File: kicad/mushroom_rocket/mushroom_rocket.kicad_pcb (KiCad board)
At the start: 2 copper layers, 69.7 x 94.5 mm, 8 parts, among them SW1 SW_DIP_x01

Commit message: 2 fixes
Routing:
- added copper zone on F.Cu, net VCC
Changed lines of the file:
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@@
 		)
 		(fp_text user "+"
-			(at 3 -4.249999 10)
+			(at 3 -4.249998 10)
 			(layer "B.SilkS")
 			(effects
@@
 	)
 	(zone
+		(net 3)
+		(net_name "VCC")
+		(layer "F.Cu")
+		(hatch edge 0.5)
+		(priority 8)
+		(connect_pads
+			(clearance 0.5)
+		)
+		(min_thickness 0.25)
+		(filled_areas_thickness no)
+		(fill yes
+			(thermal_gap 0.5)
+			(thermal_bridge_width 0.5)
+		)
+		(polygon
+			(pts
+				(xy 154 73.374) (xy 157.75 73.374) (xy 157.75 74.25) (xy 153.995 74.308)
+			)
+		)
+	)
+	(zone
+		(net 2)
+		(net_name "GND")
+		(layer "F.Cu")
+		(hatch edge 0.5)
+		(priority 7)
+		(connect_pads
+			(clearance 0.5)
+		)
+		(min_thickness 0.25)
+		(filled_areas_thickness no)
+		(fill yes
+			(thermal_gap 0.5)
+			(thermal_bridge_width 0.5)
+		)
+		(polygon
+			(pts
+				(xy 156.5 126) (xy 157 129.5) (xy 158 130.5) (xy 158.5 130.5) (xy 160 129) (xy 160.25 126) (xy 158.5 125.5)
+			)
+		)
+	)
+	(zone

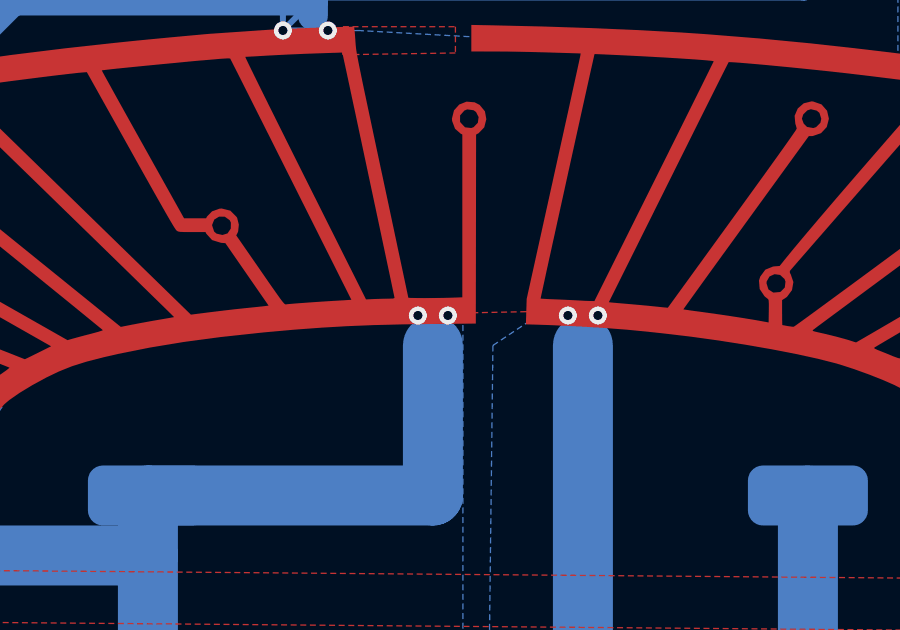
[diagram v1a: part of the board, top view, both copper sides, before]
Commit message: added a random pad into the footprint
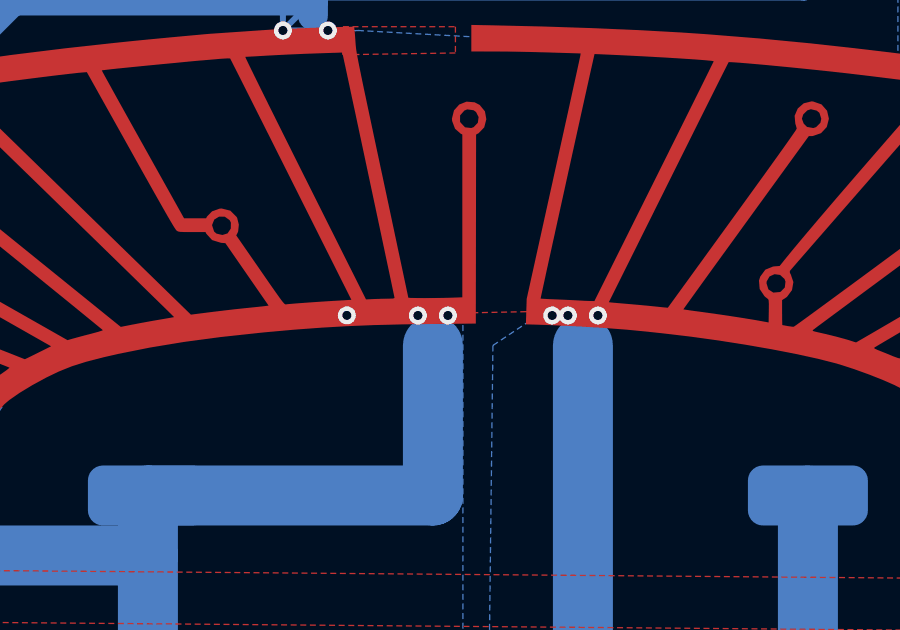
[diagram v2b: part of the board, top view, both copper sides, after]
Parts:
- ART1: renamed from REF**; value Footprint_Mushroom_v0.6 -> R
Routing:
- net VCC: vias 6 -> 7
- net GND: vias 6 -> 7
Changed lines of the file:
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@@
 		(layer "F.Cu")
 		(at 158 95)
-		(property "Reference" "REF**"
+		(property "Reference" "ART1"
 			(at 0 -0.5 0)
 			(unlocked yes)
@@
 			)
 		)
-		(property "Value" "Footprint_Mushroom_v0.6"
+		(property "Value" "R"
 			(at 0 1 0)
 			(unlocked yes)
@@
 			)
 		)
-		(property "Datasheet" ""
+		(property "Datasheet" "~"
 			(at 0 0 0)
 			(unlocked yes)
@@
 			)
 		)
-		(property "Description" ""
+		(property "Description" "Resistor"
 			(at 0 0 0)
 			(unlocked yes)
@@
 			)
 		)
+		(property ki_fp_filters "R_*")
+		(sheetname "/")
+		(sheetfile "mushroom_rocket.kicad_sch")
 		(attr smd)
 		(fp_poly
@@
 			(zone_connect 0)
 		)
+		(pad "1" smd circle
+			(at -3.85 -12.05)
+			(size 0.564 0.564)
+			(layers "F.Cu" "F.Mask" "F.Paste")
+			(net 3 "VCC")
+			(pintype "passive")
+		)
+		(pad "2" smd circle
+			(at 3.025 -12.025)
+			(size 0.564 0.564)
+			(layers "F.Cu" "F.Mask" "F.Paste")
+			(net 2 "GND")
+			(pintype "passive")
+		)
 		(embedded_fonts no)
 	)
@@
 	)
 	(via
+		(at 160.975 83)
+		(size 0.6)
+		(drill 0.3)
+		(layers "F.Cu" "B.Cu")
+		(net 2)
+	)
+	(via
 		(at 190 80)
 		(size 0.6)
@@
 		(drill 0.3)
 		(layers "F.Cu" "B.Cu")
+		(free yes)
 		(net 3)
 	)
@@
 		(net 3)
 	)
+	(via
+		(at 154.132 82.99667)
+		(size 0.6)
+		(drill 0.3)
+		(layers "F.Cu" "B.Cu")
+		(net 3)
+	)
 	(segment
 		(start 147.5 89)
@@
 			(thermal_gap 0.5)
 			(thermal_bridge_width 0.5)
+			(island_removal_mode 1)
+			(island_area_min 10)
 		)
 		(polygon

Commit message: final changes and gerber file
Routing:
- net GND: vias 7 -> 6
- removed copper zone on F.Cu, net VCC
